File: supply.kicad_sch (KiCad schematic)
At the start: 84 parts, among them U10 CSD86330Q3D, U26 74LVC1G07_SOT-753, U4 PAC1934_QFN, U5 TPS2117DRLR, U6 TPS2117DRLR, U7 LMR62014XMF, U8 TPS65086100, U9 CSD86330Q3D

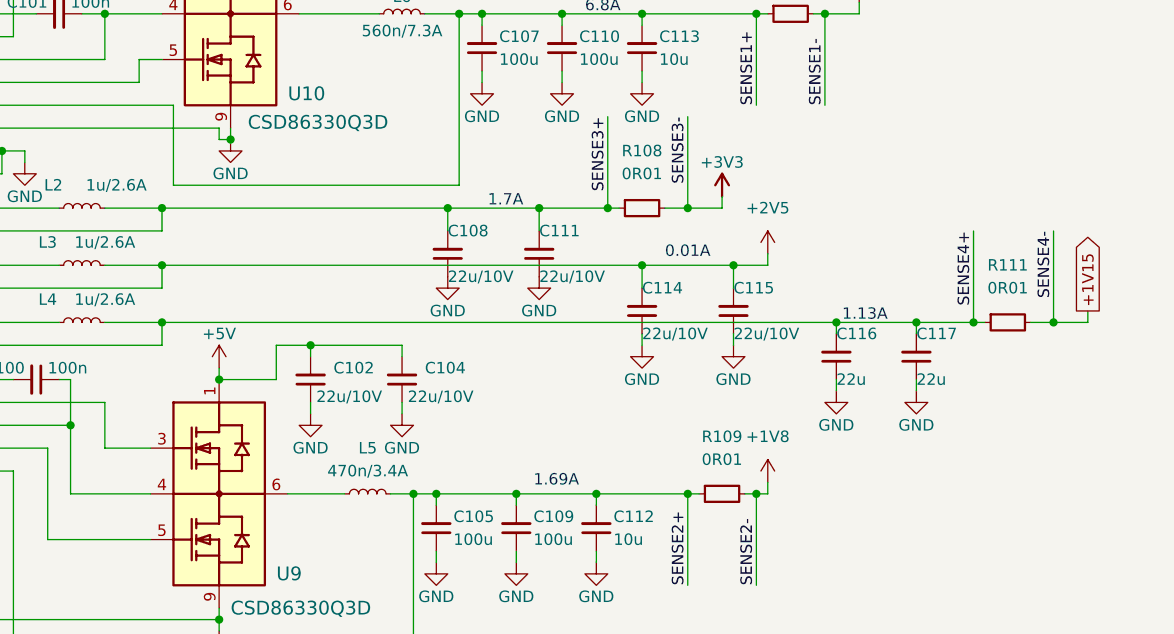
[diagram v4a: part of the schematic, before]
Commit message: [#54899] Add jumper on +2V5 line
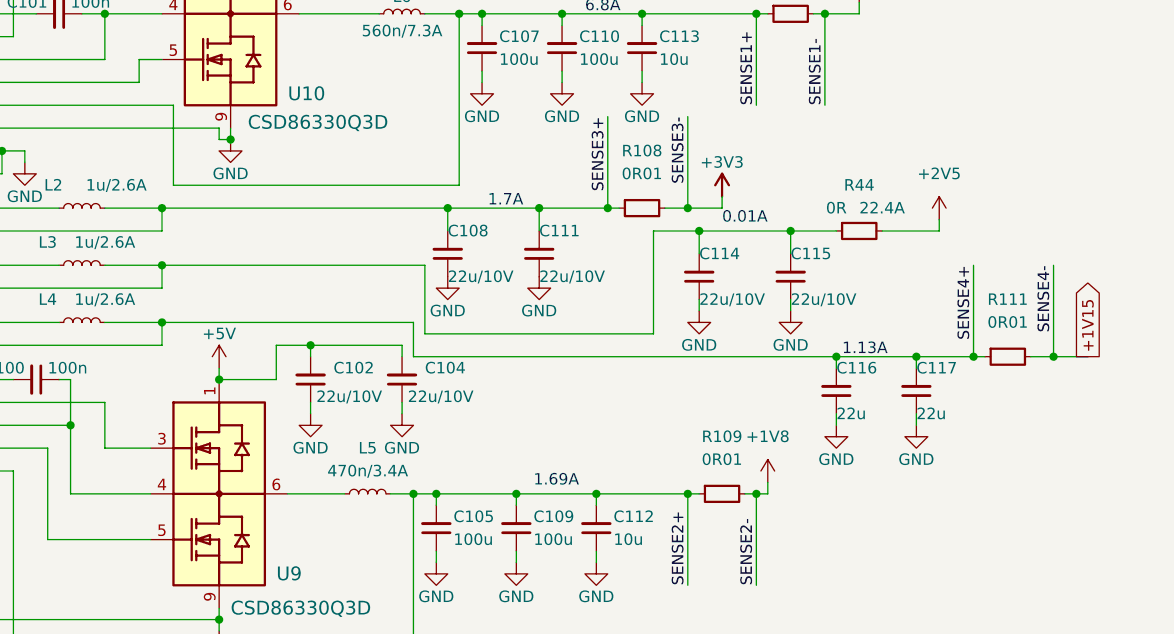
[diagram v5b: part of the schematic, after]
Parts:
- added R44: R_0R_22.4A_0603, antmicro-footprints:R_0603_1608Metric, symbol antmicroResistors0603:R_0R_22.4A_0603
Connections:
- net +2V5: now also R44.2; no longer C114.2, C115.2, L3.2, U8.23 (FB4)
- new net: C114.2, C115.2, L3.2, R44.1, U8.23 (FB4)
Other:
- moved on the sheet: C114, C115, C116, C117, R111

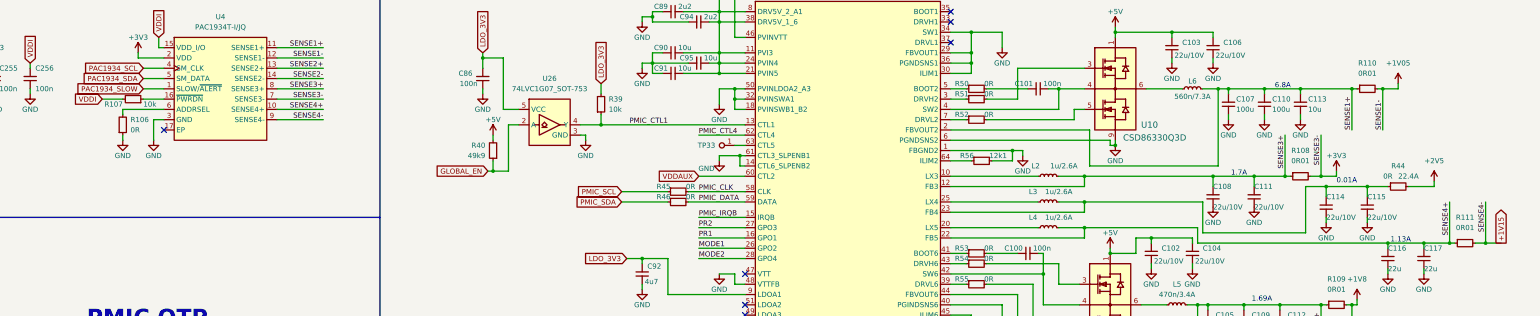
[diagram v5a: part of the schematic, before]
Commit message: [#54899] Add I2C connections
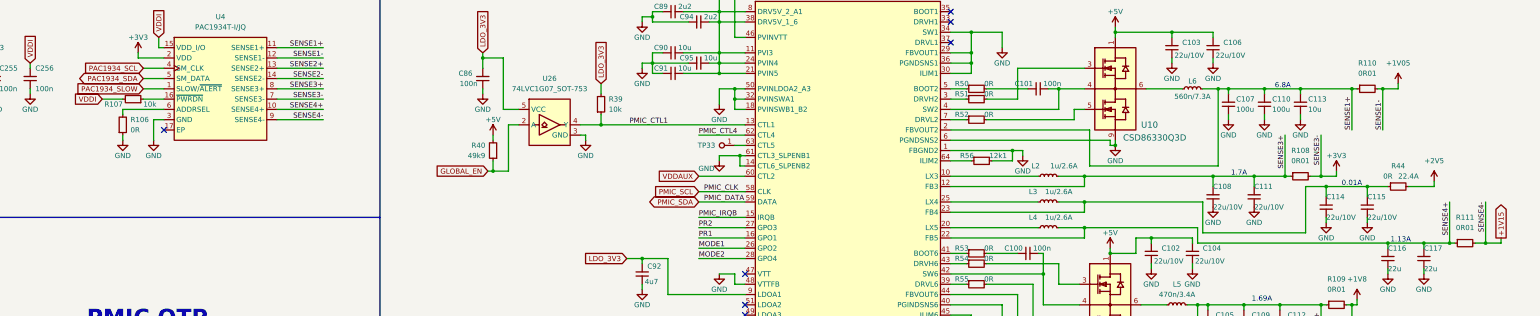
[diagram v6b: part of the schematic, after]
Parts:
- removed R45, R46: R_0R_0402, antmicro-footprints:R_0402_1005Metric, symbol antmicroResistors0402:R_0R_0402
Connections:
- net PMIC_CLK is gone; now on net PMIC_SCL: TP10.1, U8.58 (CLK)
- net PMIC_DATA is gone; now on net PMIC_SDA: TP14.1, U8.59 (DATA)

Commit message: [#54899] Re-annotate components
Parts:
- renumbered C108 to C107, C107 to C108, C111 to C110, C110 to C111, C255 to C83, C256 to C84, C86 to C85, C83 to C86, C92 to C87, C87 to C88, C88 to C89, C89 to C90, C90 to C91, C91 to C92, D2 to D1, R34 to R47, R35 to R48, R41 to R49, R42 to R50, R106 to R51, R107 to R52, R36 to R53, R37 to R54, R38 to R55, R40 to R56, R39 to R57, R43 to R58, R48 to R59, R49 to R60, R50 to R61, R51 to R62, R52 to R63, R53 to R64, R54 to R65, R55 to R66, R56 to R67, R57 to R68, R108 to R69, R109 to R70, R110 to R71, R44 to R72, R111 to R73, TP10 to TP2, TP11 to TP3, TP12 to TP4, TP13 to TP5, TP14 to TP6, TP33 to TP7, U9 to U10, U10 to U11, U5 to U4, U6 to U5, U4 to U6, U26 to U7, U7 to U8, U8 to U9

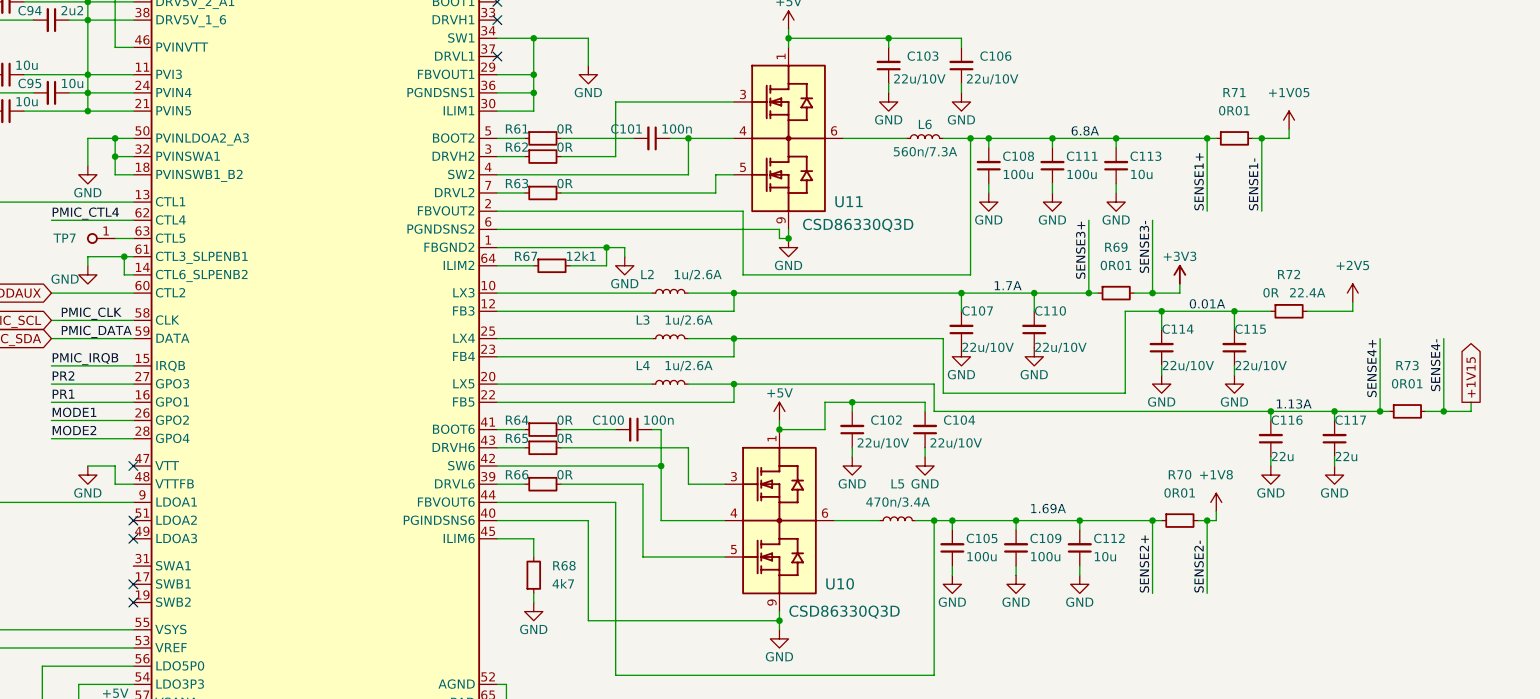
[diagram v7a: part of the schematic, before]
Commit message: [#54899] Flag not connected pins
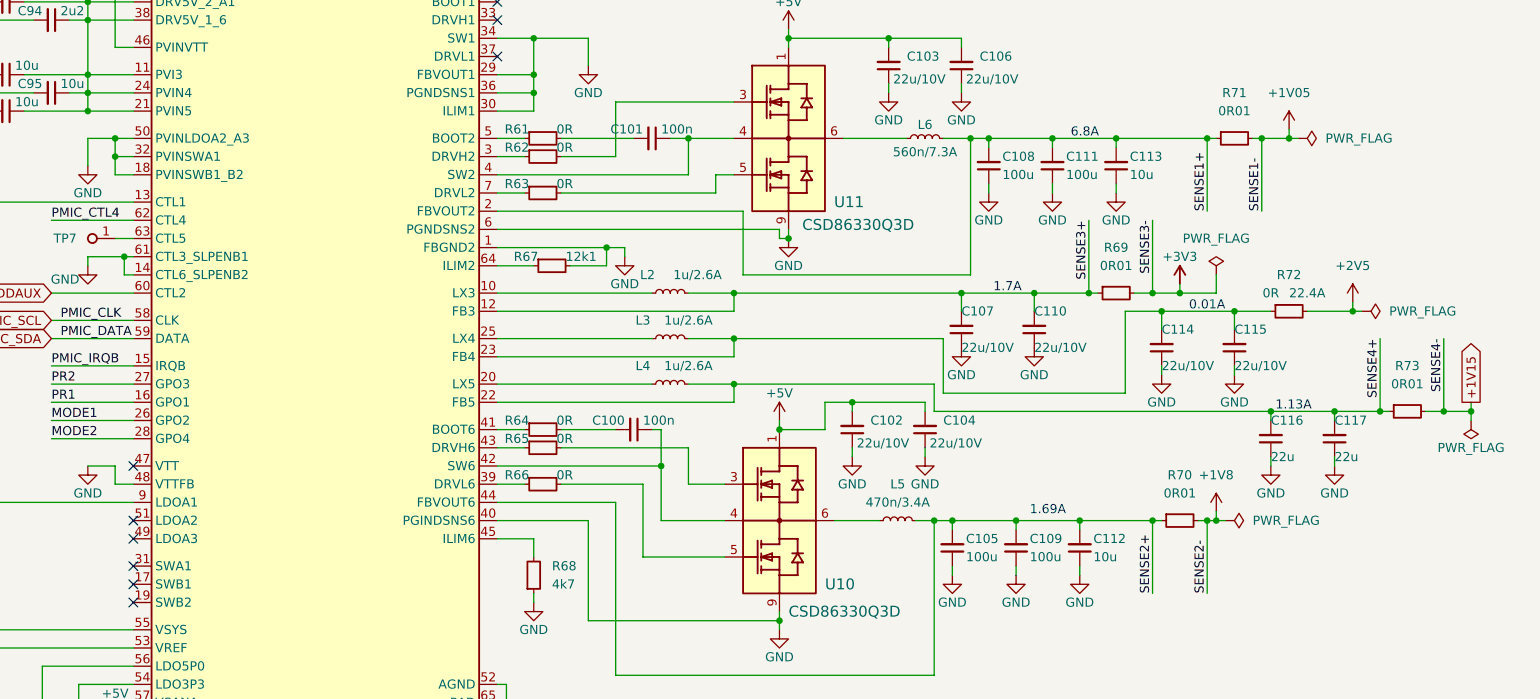
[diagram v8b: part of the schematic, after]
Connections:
- no-connect marks 10 -> 11
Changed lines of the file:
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@@
   (junction (at 332.74 60.96) (diameter 0) (color 0 0 0 0)
   )
+  (junction (at 374.65 60.96) (diameter 0) (color 0 0 0 0)
+  )
   (junction (at 318.77 46.99) (diameter 0) (color 0 0 0 0)
   )
   (junction (at 207.01 54.61) (diameter 0) (color 0 0 0 0)
   )
+  (junction (at 400.05 99.06) (diameter 0) (color 0 0 0 0)
+  )
   (junction (at 355.6 114.3) (diameter 0) (color 0 0 0 0)
   )
@@
   (junction (at 339.09 82.55) (diameter 0) (color 0 0 0 0)
   )
+  (junction (at 383.54 85.09) (diameter 0) (color 0 0 0 0)
+  )
   (junction (at 232.41 232.41) (diameter 0) (color 0 0 0 0)
   )
@@
   (junction (at 396.24 99.06) (diameter 0) (color 0 0 0 0)
   )
+  (junction (at 364.49 114.3) (diameter 0) (color 0 0 0 0)
+  )
   (junction (at 387.35 99.06) (diameter 0) (color 0 0 0 0)
   )
@@
   (junction (at 304.8 74.93) (diameter 0) (color 0 0 0 0)
   )
+  (junction (at 359.41 82.55) (diameter 0) (color 0 0 0 0)
+  )
   (junction (at 363.22 60.96) (diameter 0) (color 0 0 0 0)
   )
@@
   (no_connect (at 213.36 106.68))
   (no_connect (at 213.36 125.73))
+  (no_connect (at 213.36 120.65))
   (no_connect (at 213.36 116.84))
   (no_connect (at 82.55 247.65))
@@
     (stroke (width 0) (type default))
   )
-  (wire (pts (xy 167.64 234.95) (xy 167.64 242.57))
-    (stroke (width 0) (type default))
-  )
   (wire (pts (xy 339.09 82.55) (xy 339.09 85.09))
     (stroke (width 0) (type default))
@@
     (stroke (width 0) (type default))
   )
+  (wire (pts (xy 167.64 234.95) (xy 167.64 242.57))
+    (stroke (width 0) (type default))
+  )
   (wire (pts (xy 328.93 48.26) (xy 328.93 46.99))
     (stroke (width 0) (type default))
@@
     (stroke (width 0) (type default))
   )
+  (wire (pts (xy 374.65 60.96) (xy 375.92 60.96))
+    (stroke (width 0) (type default))
+  )
   (wire (pts (xy 264.16 106.68) (xy 287.02 106.68))
     (stroke (width 0) (type default))
@@
     (stroke (width 0) (type default))
   )
+  (wire (pts (xy 364.49 114.3) (xy 365.76 114.3))
+    (stroke (width 0) (type default))
+  )
   (wire (pts (xy 264.16 139.7) (xy 265.43 139.7))
     (stroke (width 0) (type default))
@@
     (stroke (width 0) (type default))
   )
+  (wire (pts (xy 400.05 100.33) (xy 400.05 99.06))
+    (stroke (width 0) (type default))
+  )
   (wire (pts (xy 64.77 55.88) (xy 69.85 55.88))
     (stroke (width 0) (type default))
@@
     (stroke (width 0) (type default))
   )
+  (wire (pts (xy 383.54 85.09) (xy 384.81 85.09))
+    (stroke (width 0) (type default))
+  )
   (wire (pts (xy 242.57 240.03) (xy 242.57 242.57))
     (stroke (width 0) (type default))
@@
     (stroke (width 0) (type default))
   )
+  (wire (pts (xy 364.49 82.55) (xy 359.41 82.55))
+    (stroke (width 0) (type default))
+  )
   (wire (pts (xy 177.8 69.85) (xy 213.36 69.85))
     (stroke (width 0) (type default))
@@
     (stroke (width 0) (type default))
   )
+  (wire (pts (xy 364.49 80.01) (xy 364.49 82.55))
+    (stroke (width 0) (type default))
+  )
   (wire (pts (xy 290.83 104.14) (xy 273.05 104.14))
     (stroke (width 0) (type default))
@@
     )
   )
+  (symbol (lib_id "antmicropower:PWR_FLAG") (at 365.76 114.3 270) (mirror x) (unit 1)
+    (in_bom yes) (on_board yes) (dnp no) (fields_autoplaced)
+    (property "Reference" "#FLG03" (at 367.665 114.3 0)
+      (effects (font (size 1.27 1.27)) hide)
+    )
+    (property "Value" "PWR_FLAG" (at 369.57 114.3 90)
+      (effects (font (size 1.27 1.27)) (justify left))
+    )
+    (property "Footprint" "" (at 365.76 114.3 0)
+      (effects (font (size 1.27 1.27)) hide)
+    )
+    (property "Datasheet" "" (at 365.76 114.3 0)
+      (effects (font (size 1.27 1.27)) hide)
+    )
+    (pin "1")
+    (instances
+      (project "polarfire-som"
+        (path "/db4a0d3e-2eb3-499e-977d-6eb378cfd3ed/aa0aa716-c477-450b-ad01-6403345c3aae"
+          (reference "#FLG03") (unit 1)
+        )
+      )
+    )
+  )
   (symbol (lib_id "antmicroFixedInductors:L_560n_7.3A_Bourns-SRP4020") (at 321.31 60.96 0) (unit 1)
     (in_bom yes) (on_board yes) (dnp no)
@@
     )
   )
+  (symbol (lib_id "antmicropower:PWR_FLAG") (at 364.49 80.01 0) (mirror y) (unit 1)
+    (in_bom yes) (on_board yes) (dnp no) (fields_autoplaced)
+    (property "Reference" "#FLG04" (at 364.49 78.105 0)
+      (effects (font (size 1.27 1.27)) hide)
+    )
+    (property "Value" "PWR_FLAG" (at 364.49 74.93 0)
+      (effects (font (size 1.27 1.27)))
+    )
+    (property "Footprint" "" (at 364.49 80.01 0)
+      (effects (font (size 1.27 1.27)) hide)
+    )
+    (property "Datasheet" "" (at 364.49 80.01 0)
+      (effects (font (size 1.27 1.27)) hide)
+    )
+    (pin "1")
+    (instances
+      (project "polarfire-som"
+        (path "/db4a0d3e-2eb3-499e-977d-6eb378cfd3ed/aa0aa716-c477-450b-ad01-6403345c3aae"
+          (reference "#FLG04") (unit 1)
+        )
+      )
+    )
+  )
   (symbol (lib_id "antmicroResistors0402:R_0R_0402") (at 267.97 63.5 0) (unit 1)
     (in_bom yes) (on_board yes) (dnp no)
@@
     )
   )
+  (symbol (lib_id "antmicropower:PWR_FLAG") (at 375.92 60.96 270) (mirror x) (unit 1)
+    (in_bom yes) (on_board yes) (dnp no) (fields_autoplaced)
+    (property "Reference" "#FLG01" (at 377.825 60.96 0)
+      (effects (font (size 1.27 1.27)) hide)
+    )
+    (property "Value" "PWR_FLAG" (at 379.73 60.96 90)
+      (effects (font (size 1.27 1.27)) (justify left))
+    )
+    (property "Footprint" "" (at 375.92 60.96 0)
+      (effects (font (size 1.27 1.27)) hide)
+    )
+    (property "Datasheet" "" (at 375.92 60.96 0)
+      (effects (font (size 1.27 1.27)) hide)
+    )
+    (pin "1")
+    (instances
+      (project "polarfire-som"
+        (path "/db4a0d3e-2eb3-499e-977d-6eb378cfd3ed/aa0aa716-c477-450b-ad01-6403345c3aae"
+          (reference "#FLG01") (unit 1)
+        )
+      )
+    )
+  )
   (symbol (lib_id "antmicroTransistorsFETsMOSFETsArrays:CSD86330Q3D") (at 297.18 55.88 0) (unit 1)
     (in_bom yes) (on_board yes) (dnp no)
@@
     )
   )
+  (symbol (lib_id "antmicropower:PWR_FLAG") (at 400.05 100.33 0) (mirror x) (unit 1)
+    (in_bom yes) (on_board yes) (dnp no)
+    (property "Reference" "#FLG05" (at 400.05 102.235 0)
+      (effects (font (size 1.27 1.27)) hide)
+    )
+    (property "Value" "PWR_FLAG" (at 400.05 104.14 0)
+      (effects (font (size 1.27 1.27)))
+    )
+    (property "Footprint" "" (at 400.05 100.33 0)
+      (effects (font (size 1.27 1.27)) hide)
+    )
+    (property "Datasheet" "" (at 400.05 100.33 0)
+      (effects (font (size 1.27 1.27)) hide)
+    )
+    (pin "1")
+    (instances
+      (project "polarfire-som"
+        (path "/db4a0d3e-2eb3-499e-977d-6eb378cfd3ed/aa0aa716-c477-450b-ad01-6403345c3aae"
+          (reference "#FLG05") (unit 1)
+        )
+      )
+    )
+  )
   (symbol (lib_id "antmicropower:GND") (at 341.63 68.58 0) (unit 1)
     (in_bom yes) (on_board yes) (dnp no)
@@
         )
       )
+    )
+  )
+  (symbol (lib_id "antmicropower:PWR_FLAG") (at 384.81 85.09 270) (mirror x) (unit 1)
+    (in_bom yes) (on_board yes) (dnp no) (fields_autoplaced)
+    (property "Reference" "#FLG02" (at 386.715 85.09 0)
+      (effects (font (size 1.27 1.27)) hide)
+    )
+    (property "Value" "PWR_FLAG" (at 388.62 85.09 90)
+      (effects (font (size 1.27 1.27)) (justify left))
+    )
+    (property "Footprint" "" (at 384.81 85.09 0)
+      (effects (font (size 1.27 1.27)) hide)
+    )
+    (property "Datasheet" "" (at 384.81 85.09 0)
+      (effects (font (size 1.27 1.27)) hide)
+    )
+    (pin "1")
+    (instances
+      (project "polarfire-som"
+        (path "/db4a0d3e-2eb3-499e-977d-6eb378cfd3ed/aa0aa716-c477-450b-ad01-6403345c3aae"
+          (reference "#FLG02") (unit 1)
+        )
+      )
